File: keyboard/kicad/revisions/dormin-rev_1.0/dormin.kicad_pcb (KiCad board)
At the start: 2 copper layers, 289.7 x 102.8 mm, 61 parts, among them SW1 SW_Push, SW10 SW_Push, SW11 SW_Push, SW12 SW_Push, SW13 SW_Push, SW14 SW_Push, SW15 SW_Push, SW16 SW_Push, SW17 SW_Push, SW18 SW_Push, SW19 SW_Push, SW2 SW_Push, SW20 SW_Push, SW21 SW_Push, SW22 SW_Push, SW23 SW_Push, SW24 SW_Push, SW25 SW_Push, SW26 SW_Push, SW27 SW_Push, SW28 SW_Push, SW29 SW_Push, SW3 SW_Push, SW30 SW_Push, SW31 SW_Push, SW32 SW_Push, SW33 SW_Push, SW34 SW_Push, SW35 SW_Push, SW36 SW_Push, SW37 SW_Push, SW38 SW_Push, SW39 SW_Push, SW4 SW_Push, SW40 SW_Push, SW5 SW_Push, SW6 SW_Push, SW7 SW_Push, SW8 SW_Push, SW9 SW_Push, U1 XIAO-nRF52840-SMD, U3 XIAO-nRF52840-SMD

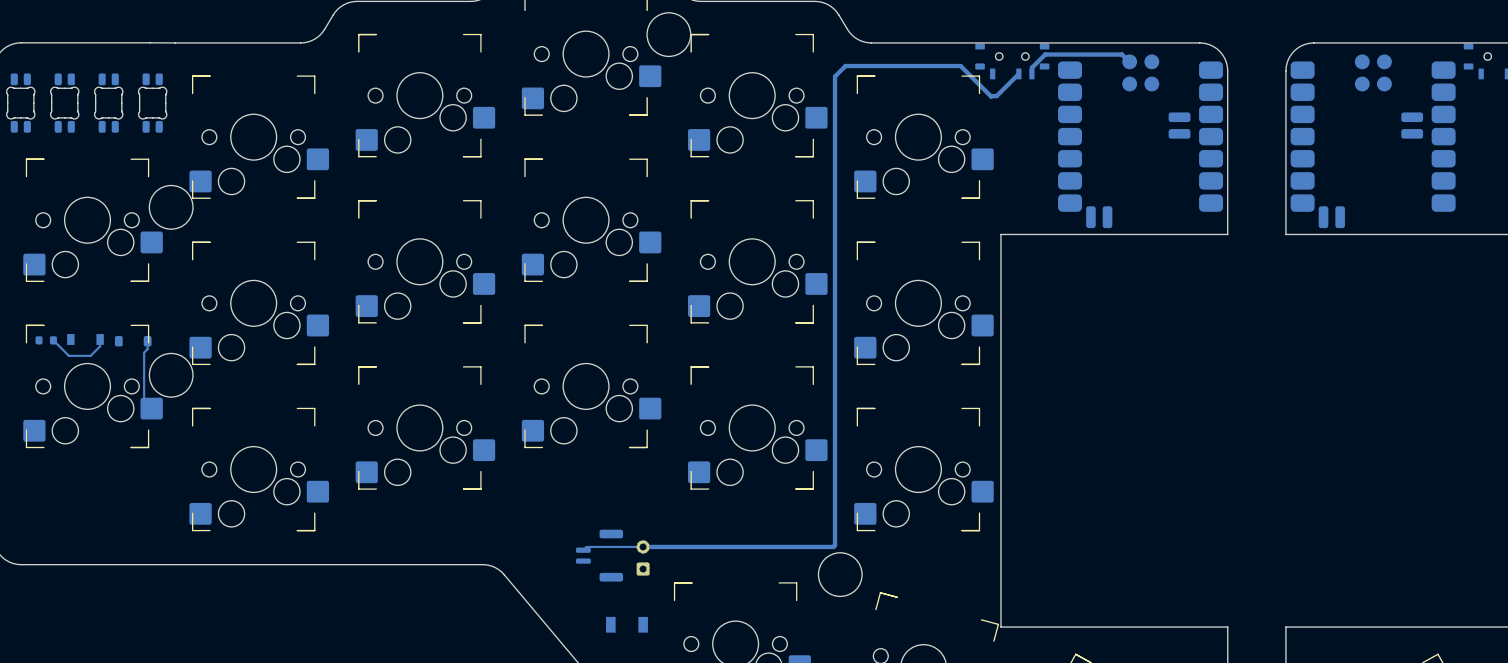
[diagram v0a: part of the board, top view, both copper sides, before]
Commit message: feat: added 3d case models and renders
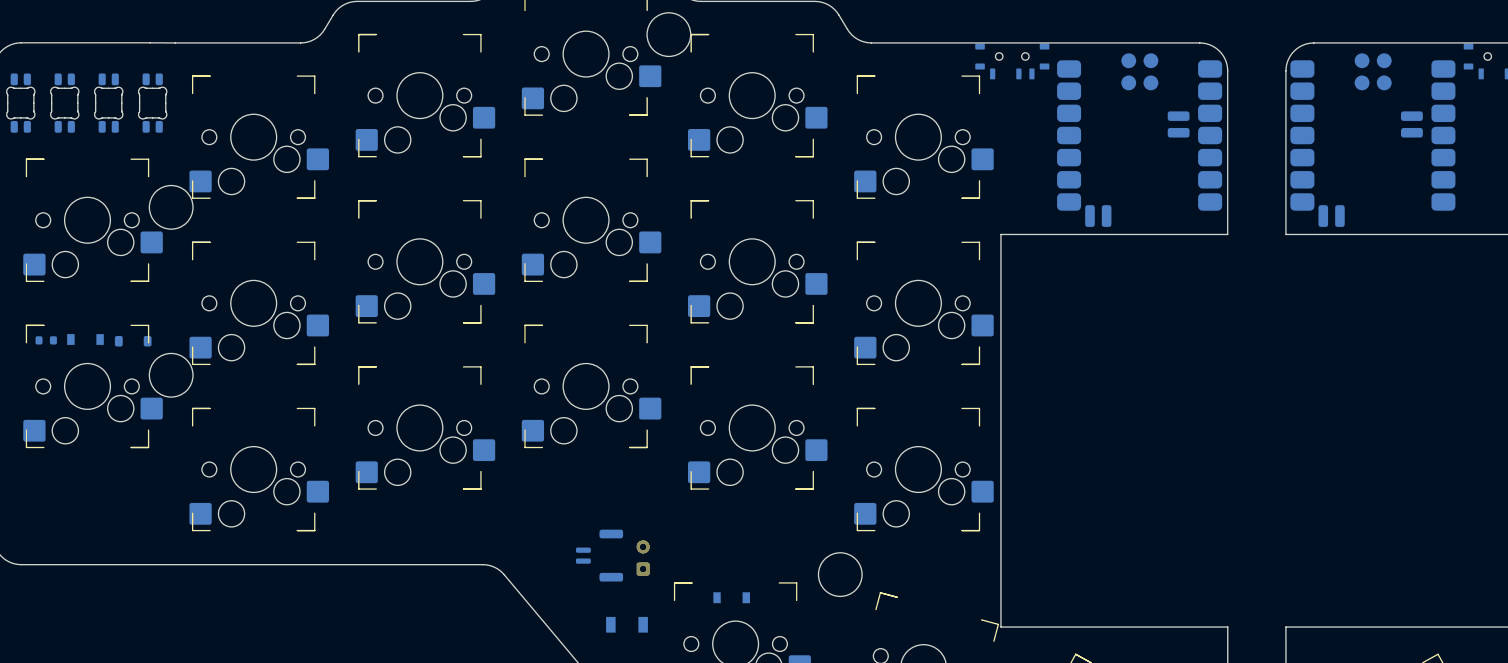
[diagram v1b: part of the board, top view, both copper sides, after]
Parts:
- added D26: LED, willkeebs_components:LED_MHT151WDT, B.Cu at (154.8, 164.7)
- moved U3 26.8 mm to (210.5, 122.2)
- moved U1 26.6 mm to (237.3, 122.2)
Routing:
- net VBAT_RAW: track 106.9 -> 0.00 mm
- net VBAT: track 12.9 -> 0.00 mm
- net Net-(D1-A): track 8.24 -> 0.00 mm
- net Net-(D25-K): track 7.32 -> 0.00 mm

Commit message: feat: added footprints | partial
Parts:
- added C1: 10uF, Capacitor_SMD:C_0603_1608Metric, B.Cu at (187.5, 120.1)
- added C2: 100nF, Capacitor_SMD:C_0603_1608Metric, B.Cu at (187.5, 118.4)
- added C3: 10uF, Capacitor_SMD:C_0603_1608Metric, B.Cu at (73.0, 103.1)
- added C4: 100nF, Capacitor_SMD:C_0603_1608Metric, B.Cu at (76.3, 103.2)
- added C5_R1: 10uF, Capacitor_SMD:C_0603_1608Metric, B.Cu at (354.5, 98.4)
- added C6_R1: 100nF, Capacitor_SMD:C_0603_1608Metric, B.Cu at (318.5, 183.6)
- added C7_R1: 10uF, Capacitor_SMD:C_0603_1608Metric, B.Cu at (318.5, 186.1)
- added C8_R1: 100nF, Capacitor_SMD:C_0603_1608Metric, B.Cu at (318.5, 188.6)
- added D10: 1N4148W, Diode_SMD:D_SOD-123, B.Cu at (143.1, 116.3)
- added D11: 1N4148W, Diode_SMD:D_SOD-123, B.Cu at (142.9, 97.3)
- added D12: 1N4148W, Diode_SMD:D_SOD-123, B.Cu at (162.1, 140.2)
- added D13: 1N4148W, Diode_SMD:D_SOD-123, B.Cu at (161.9, 120.9)
- added D14: 1N4148W, Diode_SMD:D_SOD-123, B.Cu at (162.0, 102.1)
- added D15: 1N4148W, Diode_SMD:D_SOD-123, B.Cu at (181.3, 145.0)
- added D16: 1N4148W, Diode_SMD:D_SOD-123, B.Cu at (181.2, 125.9)
- added D17: 1N4148W, Diode_SMD:D_SOD-123, B.Cu at (181.1, 106.7)
- added D18: 1N4148W, Diode_SMD:D_SOD-123, B.Cu at (160.1, 164.8)
- added D19: 1N4148W, Diode_SMD:D_SOD-123, B.Cu at (182.6, 169.0)
- added D2: 1N4148W, Diode_SMD:D_SOD-123, B.Cu at (85.8, 116.3)
- added D20: 1N4148W, Diode_SMD:D_SOD-123, B.Cu at (203.5, 178.7)
- added D29: LED, willkeebs_components:LED_MHT151WDT, B.Cu at (80.5, 116.3)
- added D3: 1N4148W, Diode_SMD:D_SOD-123, B.Cu at (105.0, 144.8)
- added D30: LED, willkeebs_components:LED_MHT151WDT, B.Cu at (99.8, 144.7)
- added D31: LED, willkeebs_components:LED_MHT151WDT, B.Cu at (99.7, 125.5)
- added D32: LED, willkeebs_components:LED_MHT151WDT, B.Cu at (99.6, 106.3)
- added D33: LED, willkeebs_components:LED_MHT151WDT, B.Cu at (118.8, 139.9)
- added D34: LED, willkeebs_components:LED_MHT151WDT, B.Cu at (118.7, 121.0)
- added D35: LED, willkeebs_components:LED_MHT151WDT, B.Cu at (118.9, 102.1)
- added D36: LED, willkeebs_components:LED_MHT151WDT, B.Cu at (137.8, 135.2)
- added D37: LED, willkeebs_components:LED_MHT151WDT, B.Cu at (137.9, 116.4)
- added D38: LED, willkeebs_components:LED_MHT151WDT, B.Cu at (137.7, 97.2)
- added D39: LED, willkeebs_components:LED_MHT151WDT, B.Cu at (156.7, 139.9)
- added D4: 1N4148W, Diode_SMD:D_SOD-123, B.Cu at (104.8, 125.6)
- added D40: LED, willkeebs_components:LED_MHT151WDT, B.Cu at (157.0, 120.8)
- added D41: LED, willkeebs_components:LED_MHT151WDT, B.Cu at (156.8, 101.8)
- added D42: LED, willkeebs_components:LED_MHT151WDT, B.Cu at (176.0, 144.9)
- added D43: LED, willkeebs_components:LED_MHT151WDT, B.Cu at (175.9, 125.8)
- added D44: LED, willkeebs_components:LED_MHT151WDT, B.Cu at (176.1, 106.6)
- added D45: LED, willkeebs_components:LED_MHT151WDT, B.Cu at (177.8, 167.6)
- added D46: LED, willkeebs_components:LED_MHT151WDT, B.Cu at (199.1, 176.1)
- added D5: 1N4148W, Diode_SMD:D_SOD-123, B.Cu at (105.1, 106.4)
- added D53_R1: LED, willkeebs_components:LED_MHT151WDT, B.Cu at (340.1, 182.4)
- added D54_R1: LED, willkeebs_components:LED_MHT151WDT, B.Cu at (340.4, 186.9)
- added D55_R1: LED, willkeebs_components:LED_MHT151WDT, B.Cu at (340.4, 191.4)
- added D56_R1: LED, willkeebs_components:LED_MHT151WDT, B.Cu at (340.4, 195.9)
- added D57_R1: LED, willkeebs_components:LED_MHT151WDT, B.Cu at (340.4, 200.4)
- added D58_R1: LED, willkeebs_components:LED_MHT151WDT, B.Cu at (334.7, 182.3)
- added D59_R1: LED, willkeebs_components:LED_MHT151WDT, B.Cu at (334.7, 186.9)
- added D6: 1N4148W, Diode_SMD:D_SOD-123, B.Cu at (124.0, 139.9)
- added D60_R1: LED, willkeebs_components:LED_MHT151WDT, B.Cu at (334.7, 191.4)
- added D61_R1: 1N4148W, Diode_SMD:D_SOD-123, B.Cu at (354.0, 135.4)
- added D62_R1: 1N4148W, Diode_SMD:D_SOD-123, B.Cu at (354.1, 116.3)
- added D63_R1: 1N4148W, Diode_SMD:D_SOD-123, B.Cu at (334.8, 144.8)
- added D64_R1: 1N4148W, Diode_SMD:D_SOD-123, B.Cu at (335.0, 125.8)
- added D65_R1: LED, willkeebs_components:LED_MHT151WDT, B.Cu at (334.7, 195.9)
- added D66_R1: LED, willkeebs_components:LED_MHT151WDT, B.Cu at (334.7, 200.4)
- added D67_R1: LED, willkeebs_components:LED_MHT151WDT, B.Cu at (329.0, 182.3)
- added D68_R1: LED, willkeebs_components:LED_MHT151WDT, B.Cu at (329.0, 186.9)
- added D69_R1: LED, willkeebs_components:LED_MHT151WDT, B.Cu at (329.0, 191.4)
- added D7: 1N4148W, Diode_SMD:D_SOD-123, B.Cu at (123.9, 121.0)
- added D70_R1: LED, willkeebs_components:LED_MHT151WDT, B.Cu at (329.0, 195.9)
- added D71_R1: LED, willkeebs_components:LED_MHT151WDT, B.Cu at (329.0, 200.4)
- added D72_R1: 1N4148W, Diode_SMD:D_SOD-123, B.Cu at (334.9, 106.8)
- added D73_R1: 1N4148W, Diode_SMD:D_SOD-123, B.Cu at (315.9, 140.2)
- added D74_R1: 1N4148W, Diode_SMD:D_SOD-123, B.Cu at (316.0, 121.1)
- added D75_R1: 1N4148W, Diode_SMD:D_SOD-123, B.Cu at (316.0, 102.1)
- added D76_R1: LED, willkeebs_components:LED_MHT151WDT, B.Cu at (323.4, 182.3)
- added D77_R1: LED, willkeebs_components:LED_MHT151WDT, B.Cu at (323.4, 186.9)
- added D78_R1: LED, willkeebs_components:LED_MHT151WDT, B.Cu at (323.4, 191.4)
- added D79_R1: LED, willkeebs_components:LED_MHT151WDT, B.Cu at (323.4, 195.9)
- added D8: 1N4148W, Diode_SMD:D_SOD-123, B.Cu at (124.0, 102.1)
- added D80_R1: LED, willkeebs_components:LED_MHT151WDT, B.Cu at (323.4, 200.4)
- added D81_R1: 1N4148W, Diode_SMD:D_SOD-123, B.Cu at (296.9, 135.4)
- added D82_R1: 1N4148W, Diode_SMD:D_SOD-123, B.Cu at (296.7, 116.4)
- added D83_R1: 1N4148W, Diode_SMD:D_SOD-123, B.Cu at (297.0, 97.5)
- added D84_R1: 1N4148W, Diode_SMD:D_SOD-123, B.Cu at (278.0, 140.1)
- added D85_R1: 1N4148W, Diode_SMD:D_SOD-123, B.Cu at (277.8, 121.0)
- added D86_R1: 1N4148W, Diode_SMD:D_SOD-123, B.Cu at (277.0, 101.2)
- added D87_R1: 1N4148W, Diode_SMD:D_SOD-123, B.Cu at (258.9, 145.0)
- added D88_R1: 1N4148W, Diode_SMD:D_SOD-123, B.Cu at (258.9, 125.9)
- added D89_R1: 1N4148W, Diode_SMD:D_SOD-123, B.Cu at (258.7, 106.7)
- added D9: 1N4148W, Diode_SMD:D_SOD-123, B.Cu at (143.1, 135.3)
- added D90_R1: 1N4148W, Diode_SMD:D_SOD-123, B.Cu at (280.0, 165.0)
- added D91_R1: 1N4148W, Diode_SMD:D_SOD-123, B.Cu at (257.1, 166.6)
- added D92_R1: 1N4148W, Diode_SMD:D_SOD-123, B.Cu at (235.1, 173.4)
- added J2: Conn_01x04, Connector_PinSocket_2.54mm:PinSocket_1x04_P2.54mm_Vertical, F.Cu at (77.3, 158.2)
- added J6_R1: Conn_01x04, Connector_PinSocket_2.54mm:PinSocket_1x04_P2.54mm_Vertical, B.Cu at (328.1, 165.4)
- added Q1: AO3400A, Package_TO_SOT_SMD:SOT-23, B.Cu at (74.2, 153.5)
- added Q2: AO3407A, Package_TO_SOT_SMD:SOT-23, B.Cu at (87.6, 153.3)
- added Q3_R1: AO3407A, Package_TO_SOT_SMD:SOT-23, B.Cu at (337.2, 165.3)
- added Q4_R1: AO3400A, Package_TO_SOT_SMD:SOT-23, B.Cu at (337.2, 169.7)
- added R10: 1K, Resistor_SMD:R_0603_1608Metric, B.Cu at (114.4, 121.0)
- added R11: 1K, Resistor_SMD:R_0603_1608Metric, B.Cu at (114.7, 102.1)
- added R12: 1K, Resistor_SMD:R_0603_1608Metric, B.Cu at (133.6, 135.4)
- added R13: 1K, Resistor_SMD:R_0603_1608Metric, B.Cu at (133.6, 116.3)
- added R14: 1K, Resistor_SMD:R_0603_1608Metric, B.Cu at (133.4, 97.3)
- added R15: 1K, Resistor_SMD:R_0603_1608Metric, B.Cu at (152.5, 140.1)
- added R16: 1K, Resistor_SMD:R_0603_1608Metric, B.Cu at (152.6, 120.8)
- added R17: 1K, Resistor_SMD:R_0603_1608Metric, B.Cu at (152.5, 101.9)
- added R18: 1K, Resistor_SMD:R_0603_1608Metric, B.Cu at (171.9, 145.1)
- added R19: 1K, Resistor_SMD:R_0603_1608Metric, B.Cu at (171.4, 125.9)
- added R2: 1K, Resistor_SMD:R_0603_1608Metric, B.Cu at (150.6, 164.7)
- added R20: 1K, Resistor_SMD:R_0603_1608Metric, B.Cu at (171.9, 106.6)
- added R21: 1K, Resistor_SMD:R_0603_1608Metric, B.Cu at (173.9, 166.5)
- added R22: 1K, Resistor_SMD:R_0603_1608Metric, B.Cu at (195.4, 174.1)
- added R25_R1: 1K, Resistor_SMD:R_0603_1608Metric, B.Cu at (318.5, 191.1)
- added R26_R1: 1K, Resistor_SMD:R_0603_1608Metric, B.Cu at (318.5, 193.6)
- added R27_R1: 1K, Resistor_SMD:R_0603_1608Metric, B.Cu at (318.5, 196.1)
- added R28_R1: 1K, Resistor_SMD:R_0603_1608Metric, B.Cu at (318.5, 198.6)
- added R29_R1: 1K, Resistor_SMD:R_0603_1608Metric, B.Cu at (314.5, 181.1)
- added R3: 1K, Resistor_SMD:R_0603_1608Metric, B.Cu at (76.3, 116.3)
- added R30_R1: 1K, Resistor_SMD:R_0603_1608Metric, B.Cu at (314.5, 183.6)
- added R31_R1: 1K, Resistor_SMD:R_0603_1608Metric, B.Cu at (314.5, 186.1)
- added R32_R1: 1K, Resistor_SMD:R_0603_1608Metric, B.Cu at (314.5, 188.6)
- added R33_R1: 1K, Resistor_SMD:R_0603_1608Metric, B.Cu at (314.5, 191.1)
- added R34_R1: 1K, Resistor_SMD:R_0603_1608Metric, B.Cu at (314.5, 193.6)
- added R35_R1: 1K, Resistor_SMD:R_0603_1608Metric, B.Cu at (314.5, 196.1)
- added R36_R1: 1K, Resistor_SMD:R_0603_1608Metric, B.Cu at (314.5, 198.6)
- added R37_R1: 1K, Resistor_SMD:R_0603_1608Metric, B.Cu at (310.5, 181.1)
- added R38_R1: 1K, Resistor_SMD:R_0603_1608Metric, B.Cu at (310.5, 183.6)
- added R39_R1: 1K, Resistor_SMD:R_0603_1608Metric, B.Cu at (310.5, 186.1)
- added R4: 1K, Resistor_SMD:R_0603_1608Metric, B.Cu at (95.2, 144.8)
- added R40_R1: 1K, Resistor_SMD:R_0603_1608Metric, B.Cu at (310.5, 188.6)
- added R41_R1: 1K, Resistor_SMD:R_0603_1608Metric, B.Cu at (310.5, 191.1)
- added R42_R1: 1K, Resistor_SMD:R_0603_1608Metric, B.Cu at (310.5, 193.6)
- added R43_R1: 1K, Resistor_SMD:R_0603_1608Metric, B.Cu at (310.5, 196.1)
- added R44_R1: 1K, Resistor_SMD:R_0603_1608Metric, B.Cu at (310.5, 198.6)
- added R7: 1K, Resistor_SMD:R_0603_1608Metric, B.Cu at (95.5, 125.6)
- added R706: 100R, Resistor_SMD:R_0603_1608Metric, B.Cu at (77.3, 153.5)
- added R707: 10k, Resistor_SMD:R_0603_1608Metric, B.Cu at (79.0, 153.5)
- added R708_R1: 100R, Resistor_SMD:R_0603_1608Metric, B.Cu at (306.5, 181.1)
- added R709_R1: 10k, Resistor_SMD:R_0603_1608Metric, B.Cu at (306.5, 183.6)
- added R710: 100R, Resistor_SMD:R_0603_1608Metric, B.Cu at (84.4, 153.5)
- added R711: 100k, Resistor_SMD:R_0603_1608Metric, B.Cu at (82.4, 153.5)
- added R712: 330R, Resistor_SMD:R_0603_1608Metric, B.Cu at (187.5, 122.0)
- added R713_R1: 100R, Resistor_SMD:R_0603_1608Metric, B.Cu at (306.5, 186.1)
- added R714_R1: 100k, Resistor_SMD:R_0603_1608Metric, B.Cu at (306.5, 188.6)
- added R715_R1: 330R, Resistor_SMD:R_0603_1608Metric, B.Cu at (306.5, 191.1)
- added R8: 1K, Resistor_SMD:R_0603_1608Metric, B.Cu at (95.5, 106.4)
- added R9: 1K, Resistor_SMD:R_0603_1608Metric, B.Cu at (114.7, 140.1)
- added TP1: VBAT, TestPoint:TestPoint_Pad_D1.0mm, B.Cu at (113.2, 158.6)
- added TP3: STS_LED_EN, TestPoint:TestPoint_Pad_D1.0mm, B.Cu at (110.1, 158.6)
- added TP4_R1: VBAT_R, TestPoint:TestPoint_Pad_D1.0mm, B.Cu at (333.2, 164.6)
- added TP6_R1: STS_LED_EN_R, TestPoint:TestPoint_Pad_D1.0mm, B.Cu at (333.2, 167.6)
- turned D25 to 0 degrees
- turned SW32 to 180 degrees
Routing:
- net VBAT_RAW_R: track 0.00 -> 105.0 mm
- net VBAT_RAW: track 0.00 -> 103.0 mm
- net GND_R: track 0.00 -> 28.5 mm, vias 0 -> 1
- net GND: track 0.00 -> 24.6 mm, vias 0 -> 1
- net VBAT_R: track 0.00 -> 23.2 mm
- net VBAT: track 0.00 -> 21.8 mm
- net Net-(D1-A): track 0.00 -> 7.91 mm
- net RESET_R: track 0.00 -> 6.20 mm
- net RESET: track 0.00 -> 6.20 mm
- net Net-(D25-K): track 0.00 -> 2.04 mm

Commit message: feat: organize footprints
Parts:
- moved D70_R1 109.6 mm to (272.5, 102.0), turned to 0 degrees
- moved D77_R1 106.3 mm to (253.5, 106.7), turned to 0 degrees
- moved R41_R1 104.5 mm to (249.0, 106.7)
- moved R35_R1 102.6 mm to (287.4, 97.2)
- moved C8_R1 102.0 mm to (242.8, 120.4)
- moved C7_R1 99.2 mm to (242.8, 122.0)
- moved R715_R1 96.5 mm to (242.8, 118.7)
- moved D80_R1 96.2 mm to (230.3, 176.4), turned to 29 degrees
- moved D66_R1 94.6 mm to (291.6, 116.2), turned to 0 degrees
- moved D57_R1 94.2 mm to (329.7, 106.8), turned to 0 degrees
- moved D71_R1 93.8 mm to (253.5, 144.8), turned to 0 degrees
- moved D67_R1 93.0 mm to (291.5, 97.2), turned to 0 degrees
- moved D60_R1 92.4 mm to (310.6, 102.1), turned to 0 degrees
- moved R38_R1 91.9 mm to (268.2, 102.1)
- moved D69_R1 90.2 mm to (272.5, 121.1), turned to 0 degrees
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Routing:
- net Net-(D47_R1-VDD): track 0.00 -> 100.1 mm
- net Net-(D21-VDD): track 0.00 -> 94.2 mm, vias 0 -> 2
- net Net-(D48_R1-DOUT): track 0.00 -> 16.9 mm
- net Net-(D50_R1-DOUT): track 0.00 -> 16.6 mm, vias 0 -> 2
- net Net-(D21-DOUT): track 0.00 -> 15.7 mm
- net Net-(D22-DOUT): track 0.00 -> 15.0 mm, vias 0 -> 2
- net GND: track 24.6 -> 39.4 mm, vias 1 -> 7
- net Net-(D23-DOUT): track 0.00 -> 14.7 mm, vias 0 -> 2
- net Net-(D47_R1-DOUT): track 0.00 -> 12.4 mm, vias 0 -> 2
- net Net-(D18-A): track 0.00 -> 10.5 mm
- net Net-(D15-A): track 0.00 -> 10.2 mm
- net Net-(D4-A): track 0.00 -> 9.69 mm
- net Net-(D5-A): track 0.00 -> 9.66 mm
- net GND_R: track 28.5 -> 38.2 mm, vias 1 -> 10
- net Net-(D13-A): track 0.00 -> 9.60 mm
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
